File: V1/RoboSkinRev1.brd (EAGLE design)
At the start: 34.3 x 12.7 mm, 11 parts, among them U4 LSM6DS3DOT_INDICATION, U5 VL53L1XSMD

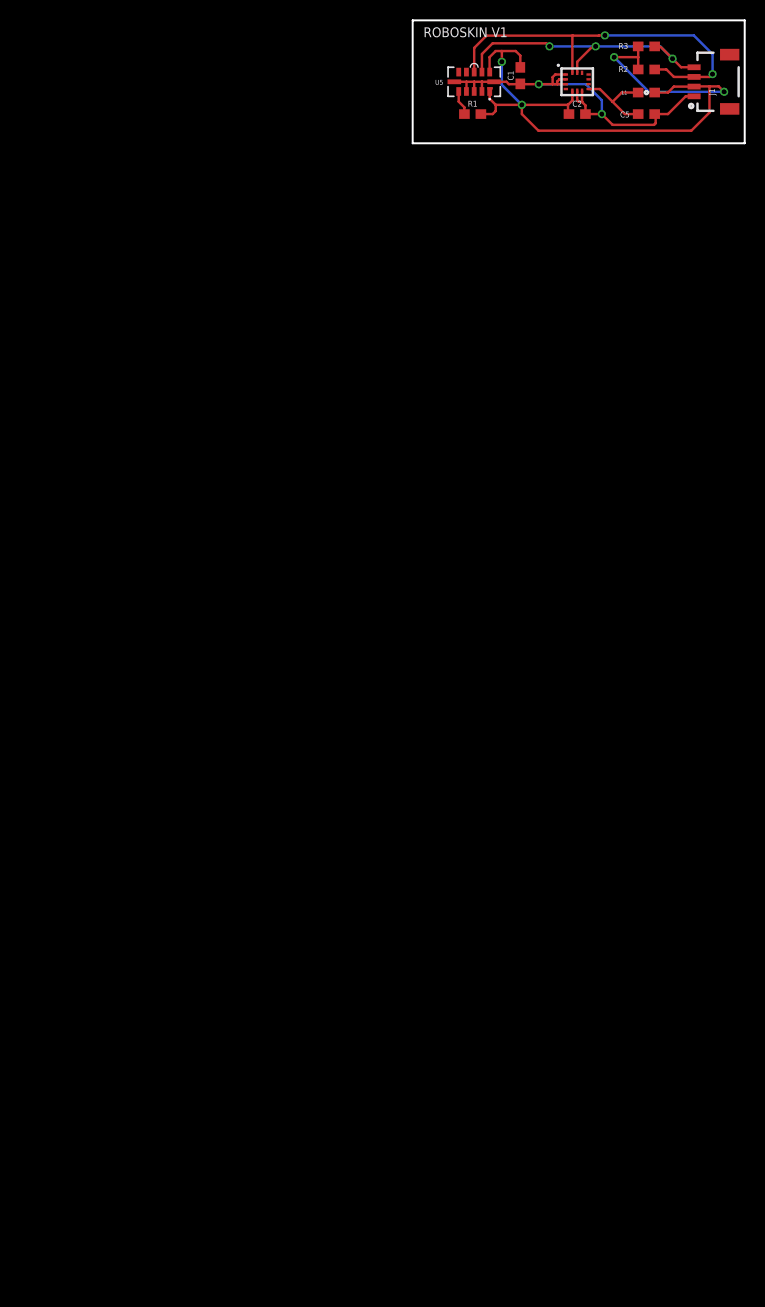
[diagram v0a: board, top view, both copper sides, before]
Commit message: Updated schematics with new sensors and supporting circuitry
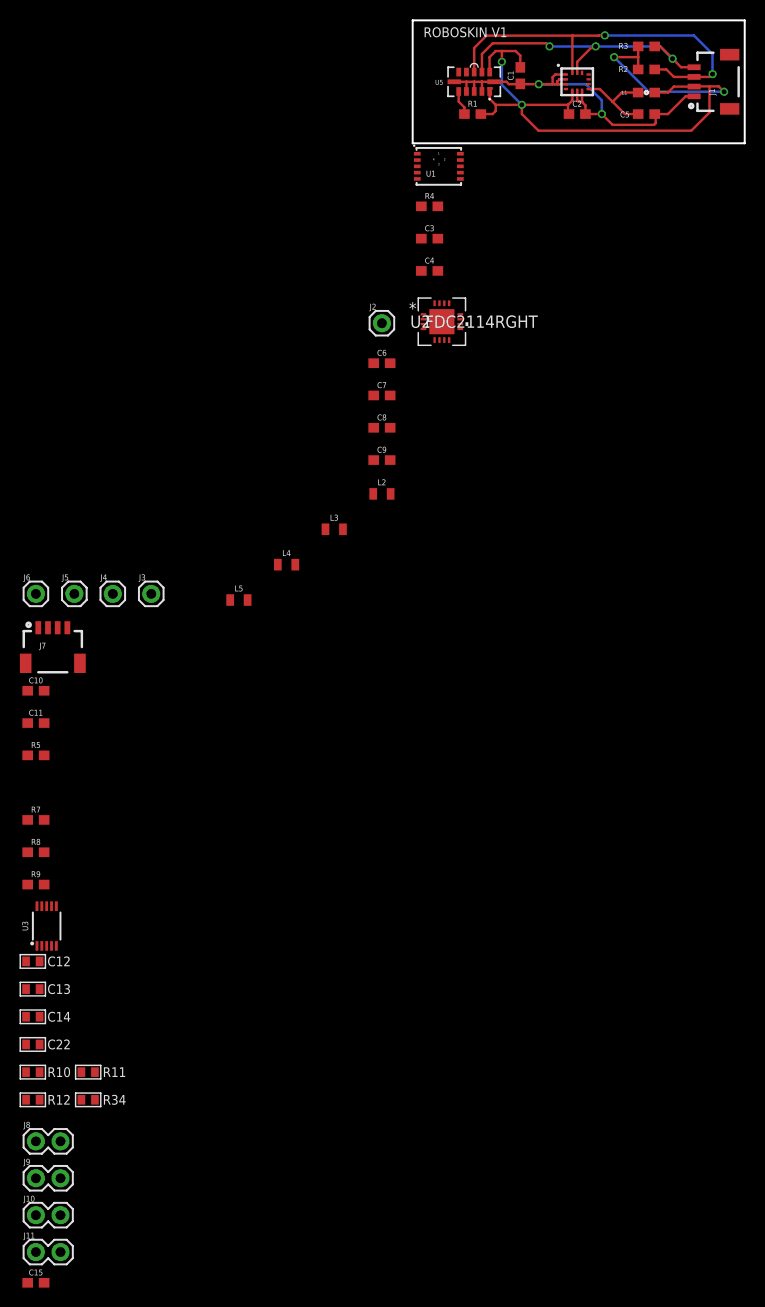
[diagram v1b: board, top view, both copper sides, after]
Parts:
- added C10, C15: 0.1uF, SparkFun-Capacitors:0603
- added C11, C3, C4: 1.0uF, SparkFun-Capacitors:0603
- added C12, C13, C14, C22: 0.1uF, 1_BES_Passives:0603_SILK
- added C6, C7, C8, C9: 33pF, SparkFun-Capacitors:0603
- added FRAME1: FRAME-LETTERNO_PACKAGE, SparkFun-Aesthetics:DUMMY
- added J10, J11, J8, J9: (no value), SparkFun-Connectors:1X02
- added J2, J3, J4, J5, J6: (no value), SparkFun-Connectors:1X01
- added J7: (no value), SparkFun-Connectors:1X04_1MM_RA
- added L2, L3, L4, L5: 10μH_SHIELDED_INDUCTOR0805, SparkFun-Coils:0805
- added R10, R11, R12, R34: 10K, 1_BES_Passives:0603_SILK
- added R4: 330, SparkFun-Resistors:0603
- added R5, R7, R8, R9: 3.3k, SparkFun-Resistors:0603
- added U1: AK9750, SparkFun-Sensors:SON10
- added U2: FDC2114RGHT, FDC2114:RGH16
- added U3: ADS1015, SparkFun-IC-Conversion:MSOP10
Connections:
- new net 0: J10.1, R12.P2, R8.1
- new net 1: J8.1, R10.P2, R9.1
- new net 2: J9.1, R11.P2, R5.1
- new net 3: J11.1, R34.P2, R7.1
- new net A0: C14.P1, R12.P1, U3.4
- new net A1: C12.P1, R10.P1, U3.5
- new net A2: C13.P1, R11.P1, U3.6
- new net A3: C22.P1, R34.P1, U3.7
- new net INT: J2.1, U2.5
- new net N$1: C4.1, R4.1, U1.1
- new net N$10: C7.2, L3.2, U2.13
- new net N$12: C8.2, L4.2, U2.11
- new net N$14: C9.2, L5.2, U2.9
- new net N$2: C3.1, U1.5, U1.8
- new net N$8: C6.2, L2.2, U2.15
- new net PAD1: C9.1, J3.1, L5.1, U2.10
- new net PAD2: C8.1, J4.1, L4.1, U2.12
- new net PAD3: C7.1, J5.1, L3.1, U2.14
- new net PAD4: C6.1, J6.1, L2.1, U2.16
- net 3.3V: now also C10.1, C11.1, C15.1, J10.2, J11.2, J7.2, J8.2, J9.2, R4.2, U2.7, U3.1, U3.8
- net GND: now also C10.2, C11.2, C12.P2, C13.P2, C14.P2, C15.2, C22.P2, C3.2, C4.2, J7.1, R5.2, R7.2, R8.2, R9.2, U1.10, U1.2, U1.3, U1.9, U2.17, U2.3, U2.4, U2.6, U2.8, U3.3
- net SCL: now also J7.4, U1.7, U2.1, U3.10
- net SDA: now also J7.3, U1.6, U2.2, U3.9
